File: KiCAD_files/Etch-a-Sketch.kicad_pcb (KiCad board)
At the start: 2 copper layers, 30 parts, among them J1 Debug Connector, J2 Display / Mounting Socket, J3 Display Mounting Socket, U1 STM32L433CCTx, U2 W25Q64JV, U3 ICM-42688-P, U4 TPS61201DRC, U5 Battery Holder, U6 Adafruit 377 Rotary Encoder, U7 Adafruit 377 Rotary Encoder

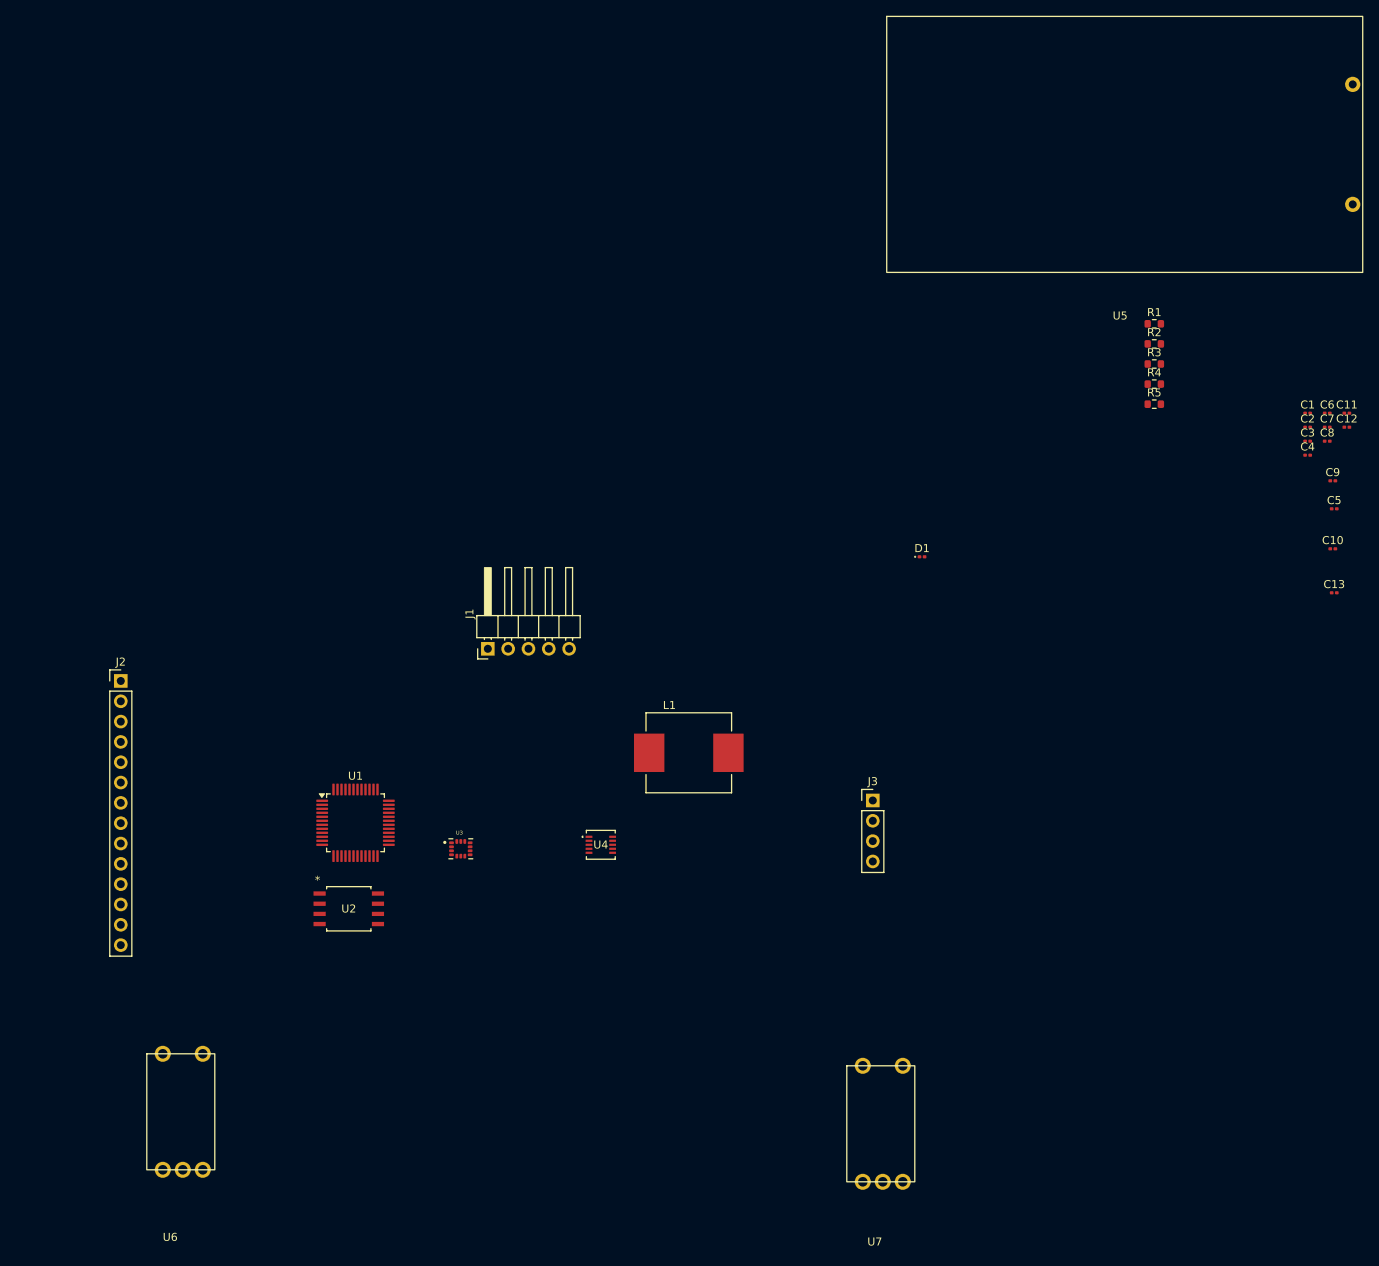
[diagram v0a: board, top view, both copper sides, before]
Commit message: Add footprints and 3D models, initial component layout, hardware improvements
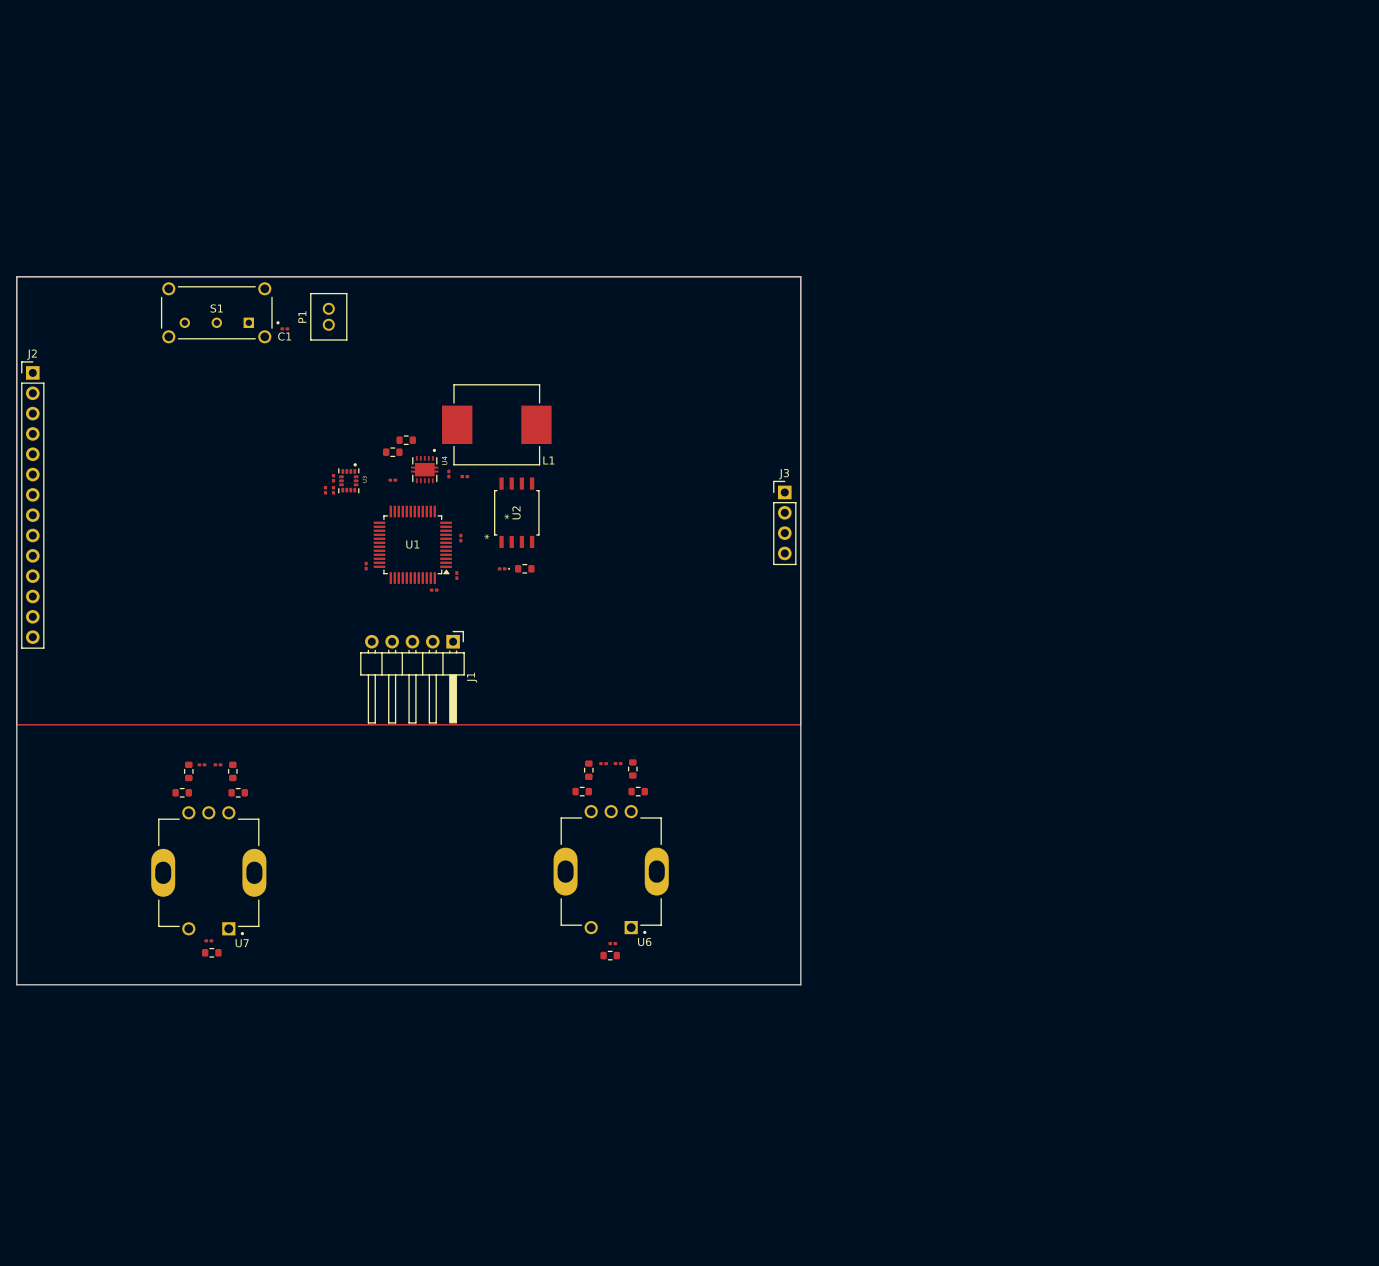
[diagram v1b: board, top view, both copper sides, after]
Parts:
- removed U5: Battery Holder, Etch_a_sketch_footprints:AA_Battery_Holder
- added C14: 0.22uF, Capacitor_SMD:C_0201_0603Metric, F.Cu at (78.7, 127.5)
- added C15: 0.22uF, Capacitor_SMD:C_0201_0603Metric, F.Cu at (76.7, 127.5)
- added C16: 0.22uF, Capacitor_SMD:C_0201_0603Metric, F.Cu at (126.8, 127.3)
- added C17: 0.22uF, Capacitor_SMD:C_0201_0603Metric, F.Cu at (128.7, 127.3)
- added P1: PHR-2, PHR_2:JST_PHR-2, F.Cu at (92.5, 71.5)
- added R10: 10k, Resistor_SMD:R_0603_1608Metric, F.Cu at (80.5, 128.3)
- added R11: 10k, Resistor_SMD:R_0603_1608Metric, F.Cu at (81.2, 131.0)
- added R12: 10k, Resistor_SMD:R_0603_1608Metric, F.Cu at (131.2, 130.8)
- added R13: 10k, Resistor_SMD:R_0603_1608Metric, F.Cu at (130.5, 128.0)
- added R6: 10k, Resistor_SMD:R_0603_1608Metric, F.Cu at (124.2, 130.8)
- added R7: 10k, Resistor_SMD:R_0603_1608Metric, F.Cu at (125.0, 128.2)
- added R8: 10k, Resistor_SMD:R_0603_1608Metric, F.Cu at (75.0, 128.3)
- added R9: 10k, Resistor_SMD:R_0603_1608Metric, F.Cu at (74.2, 131.0)
- added S1: EG1224, EG1224:SW_EG1224, F.Cu at (78.5, 71.0)
- U4: footprint tps_footprints:DRC10_2P4X1P65 -> TPS61201DRCT:VREG_V62_16624-01YE
- U6, U7: footprint Etch_a_sketch_footprints:Untitled -> PEC11R_4215F_S0024:XDCR_PEC11R-4215F-S0024
- moved C9 151.8 mm to (77.5, 149.5)
- moved R5 136.3 mm to (77.9, 151.0)
- moved C1 128.3 mm to (87.0, 73.0)
- moved C6 125.6 mm to (92.1, 93.2), turned to 90 degrees
- moved C5 125.1 mm to (93.1, 93.2), turned to 90 degrees
- moved C4 121.8 mm to (93.1, 91.7), turned to -90 degrees
- moved C10 120.8 mm to (97.2, 102.7), turned to 90 degrees
- moved C3 114.5 mm to (100.5, 91.9)
- moved C7 113.5 mm to (105.7, 105.7), turned to 180 degrees
- moved C12 112.8 mm to (108.5, 103.8), turned to -90 degrees
- moved C11 111.8 mm to (109.0, 99.2), turned to -90 degrees
- moved C13 109.6 mm to (109.5, 91.5), turned to 180 degrees
- moved C8 109.2 mm to (128.0, 149.8)
- moved C2 107.5 mm to (107.5, 91.2), turned to -90 degrees
- moved R4 98.6 mm to (127.7, 151.3), turned to 180 degrees
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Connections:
- J1 pad 2: /DEBUG_CLK -> /NRST
- J1 pad 3: /DEBUG_DIO -> /DEBUG_CLK
- J1 pad 4: /NRST -> /DEBUG_DIO
- U6 pad 1: /QEI2_A -> GND
- U6 pad 2: GND -> Net-(U6-PB_2)
- U7 pad 1: /QEI1_A -> GND
- U7 pad 2: GND -> Net-(U7-PB_2)
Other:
- board outline added: 98 x 88.5 mm
- board text added: "R10"

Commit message: Initial PCB Layout
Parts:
- added R14: 0, Resistor_SMD:R_0603_1608Metric, F.Cu at (65.2, 98.5)
- added R15: 0, Resistor_SMD:R_0603_1608Metric, F.Cu at (65.2, 96.5)
- L1: footprint SPM10040T_2R2M:IND_SPM10040T-2R2M -> LPS3015-222MRC:IND_LPS3015-222MRC
- U4: value TPS61201DRC -> ~
- moved C1 29.2 mm to (112.0, 88.1), turned to -90 degrees
- moved C3 18.0 mm to (118.0, 88.1), turned to -90 degrees
- moved C12 16.7 mm to (99.2, 89.9), turned to 180 degrees
- moved U2 14.9 mm to (105.4, 85.6), turned to 180 degrees
- moved R2 14.7 mm to (114.7, 92.4), turned to 0 degrees
- moved R1 10.8 mm to (111.5, 92.4), turned to 0 degrees
- moved C13 10.6 mm to (99.7, 87.4)
- moved C2 10.2 mm to (117.3, 88.1)
- moved U4 10.1 mm to (114.5, 88.9)
- moved R3 7.03 mm to (113.1, 97.2)
- moved D1 6.95 mm to (110.4, 97.2)
- moved C7 6.64 mm to (108.2, 99.5), turned to 0 degrees
- moved C10 5.08 mm to (97.7, 97.6)
- moved C11 5.08 mm to (109.5, 94.1)
- moved U1 5.08 mm to (103.5, 94.9)
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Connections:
- J2 pad 8: /LED -> Net-(J2-Pin_8)
- U3 pad 10: unconnected-(U3-RESV-Pad10) -> GND
- U3 pad 2: unconnected-(U3-RESV-Pad2) -> GND
- U3 pad 3: unconnected-(U3-RESV-Pad3) -> GND
- U4 pad 11: (no net) -> GND
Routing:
- net +3V3: track 0.00 -> 231.2 mm, vias 0 -> 11
- net /PB_1: track 0.00 -> 73.1 mm, vias 0 -> 2
- net GND: track 0.00 -> 69.3 mm, vias 0 -> 3
- net /SPI3_CS: track 0.00 -> 68.6 mm, vias 0 -> 1
- net /PB_2: track 0.00 -> 67.7 mm
- net /DC/RS: track 0.00 -> 63.9 mm, vias 0 -> 1
- net /SPI3_MOCI: track 0.00 -> 58.2 mm, vias 0 -> 1
- net /RESET: track 0.00 -> 56.8 mm
- net /QEI1_B: track 0.00 -> 56.3 mm, vias 0 -> 2
- net /QEI2_A: track 0.00 -> 54.9 mm, vias 0 -> 2
- net /QEI2_B: track 0.00 -> 54.0 mm, vias 0 -> 2
- net /QEI1_A: track 0.00 -> 53.3 mm, vias 0 -> 2
- net /SPI3_SCK: track 0.00 -> 52.5 mm, vias 0 -> 2
- net /SPI3_MICO: track 0.00 -> 49.8 mm
- net /LED: track 0.00 -> 47.3 mm, vias 0 -> 2
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- added copper zone on F.Cu, net GND
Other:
- board size 98 x 88.5 mm -> 98 x 85.5 mm

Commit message: PCB layout draft and clean files
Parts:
- C1, C10, C11, C12, C13, C14, C15, C16, C17, C2, C3, C4, C5, C6, C7, C8, C9: footprint Capacitor_SMD:C_0201_0603Metric -> Capacitor_SMD:C_0603_1608Metric
- J2: footprint Connector_PinHeader_2.54mm:PinHeader_1x14_P2.54mm_Vertical -> Connector_PinSocket_2.54mm:PinSocket_1x14_P2.54mm_Vertical
- J3: footprint Connector_PinHeader_2.54mm:PinHeader_1x04_P2.54mm_Vertical -> Connector_PinSocket_2.54mm:PinSocket_1x04_P2.54mm_Vertical
- P1: value PHR-2 -> 282837-2; footprint PHR_2:JST_PHR-2 -> 282837_2:TE_282837-2
- moved S1 81.4 mm to (158.6, 56.5)
- moved P1 80.8 mm to (171.8, 56.4), turned to 180 degrees
- moved C3 54.6 mm to (170.8, 74.2)
- moved R11 54.2 mm to (133.0, 115.6)
- moved R10 54.2 mm to (132.2, 113.2)
- moved R12 54.1 mm to (183.3, 115.5)
- moved R13 54.0 mm to (182.5, 113.2)
- moved C2 53.7 mm to (169.2, 74.2)
- moved C11 53.6 mm to (161.3, 80.3)
- moved C14 53.6 mm to (129.9, 112.0)
- moved C17 53.6 mm to (180.2, 112.0)
- moved C9 53.3 mm to (131.6, 134.5)
- moved C8 53.3 mm to (176.8, 134.0)
- moved C13 53.2 mm to (150.6, 72.1), turned to 90 degrees
- moved C7 53.1 mm to (159.3, 85.2)
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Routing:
- net Net-(U4-EN): track 16.8 -> 29.8 mm, vias 4 -> 2
- net Net-(P1-Pad2): track 0.00 -> 11.7 mm
- net +3V3: track 231.2 -> 237.7 mm
- net GND: track 69.3 -> 63.8 mm, vias 3 -> 6
- net /QEI1_A: track 53.3 -> 52.0 mm
- net /QEI1_B: track 56.3 -> 57.4 mm
- net Net-(U4-VAUX): track 1.87 -> 2.87 mm
- net /QEI2_A: track 54.9 -> 55.9 mm
- net /QUADSPI_IO1: track 8.39 -> 9.08 mm
- net Net-(U7-Quad_B): track 3.65 -> 4.20 mm
- net Net-(U6-Quad_A): track 3.58 -> 4.11 mm

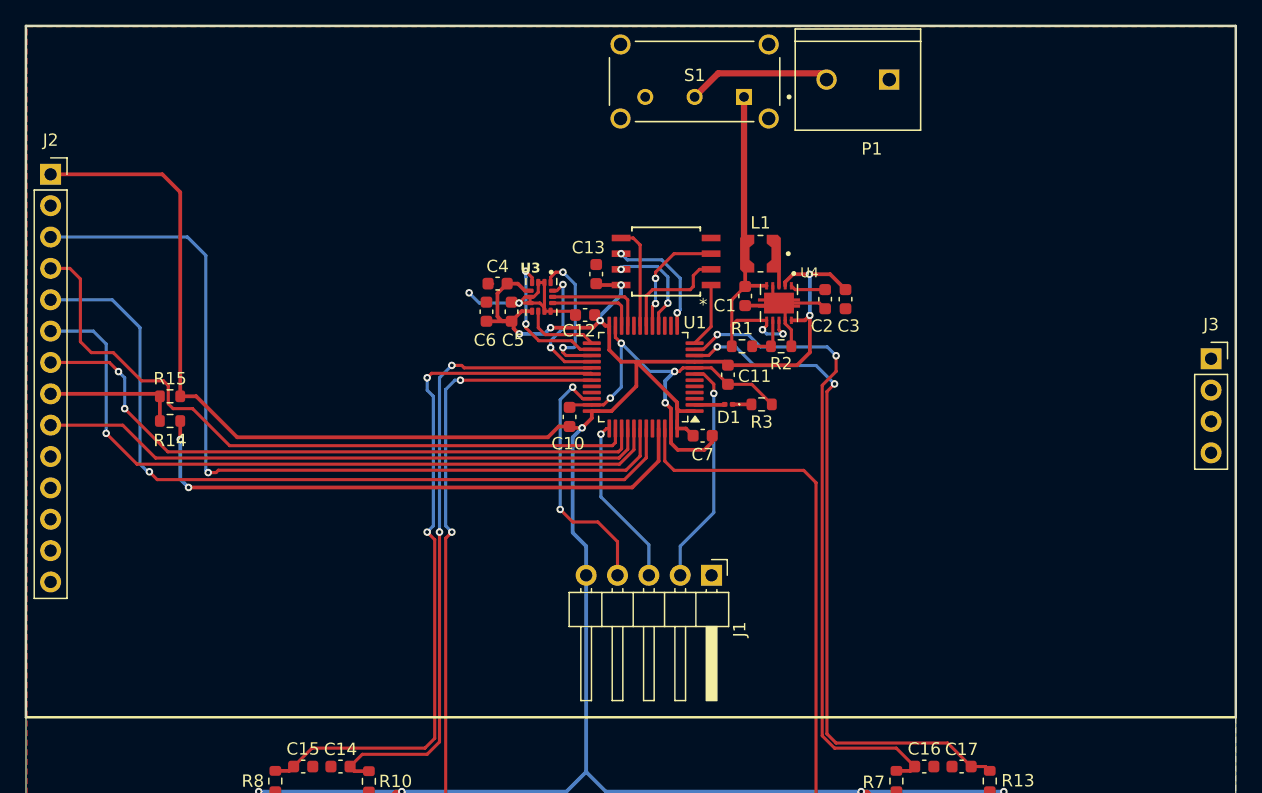
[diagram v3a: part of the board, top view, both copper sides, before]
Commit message: Final KiCAD updates, and begin driver developpment
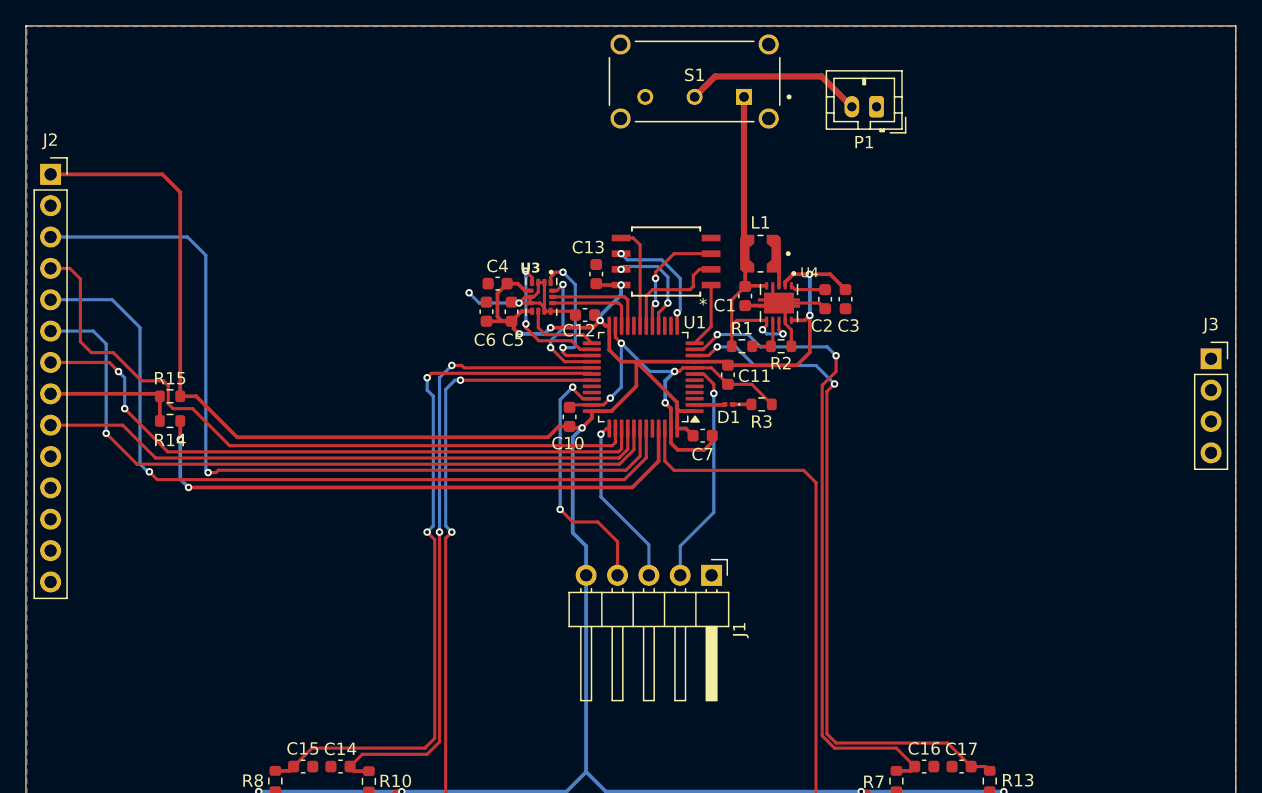
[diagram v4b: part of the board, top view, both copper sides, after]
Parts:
- P1: footprint 282837_2:TE_282837-2 -> Connector_JST:JST_PH_B2B-PH-K_1x02_P2.00mm_Vertical
- moved P1 2.67 mm to (173.3, 58.6)
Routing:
- net Net-(P1-Pad2): track 11.7 -> 14.4 mm
